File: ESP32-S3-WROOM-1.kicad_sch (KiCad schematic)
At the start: 24 parts, among them J11 Conn_01x08, J13 Conn_02x09_Top_Bottom, J14 Conn_01x09, J15 Conn_02x09_Top_Bottom, J4 JST-XH, J6 Conn_01x09, J7 Conn_02x20_Counter_Clockwise, J8 Conn_01x08, J9 Conn_01x08, SW4 SW_Push, U8 ESP32-S3-WROOM-1-N8R2

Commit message: Finished new board
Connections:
- net +5V: now also J4.4; no longer J4.1
- net Earth: now also J4.1; no longer J4.4
- net Pico_SCL1: now also U8.25 (GPIO48/SPICLK_N/SUBSPICLK_N_DIFF); no longer U8.26 (GPIO45)
- net Pico_SDA1: now also U8.26 (GPIO45); no longer U8.25 (GPIO48/SPICLK_N/SUBSPICLK_N_DIFF)
- net SCL: now also J4.3; no longer J4.2
- net SDA: now also J4.2; no longer J4.3
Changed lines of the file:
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@@
 	(wire
 		(pts
+			(xy 269.24 146.05) (xy 269.24 154.94)
+		)
+		(stroke
+			(width 0)
+			(type default)
+		)
+	)
+	(wire
+		(pts
 			(xy 143.51 59.69) (xy 149.86 59.69)
 		)
@@
 	(wire
 		(pts
-			(xy 269.24 146.05) (xy 269.24 154.94)
-		)
-		(stroke
-			(width 0)
-			(type default)
-		)
-	)
-	(wire
-		(pts
 			(xy 45.72 67.31) (xy 46.99 67.31)
 		)
@@
 	(global_label "Pico_SCL1"
 		(shape input)
-		(at 260.35 102.87 0)
+		(at 260.35 110.49 0)
 		(fields_autoplaced yes)
 		(effects
@@
 		)
 		(property "Intersheetrefs" "${INTERSHEET_REFS}"
-			(at 273.1323 102.87 0)
+			(at 273.1323 110.49 0)
 			(effects
 				(font
@@
 	(global_label "Pico_SDA1"
 		(shape input)
-		(at 260.35 110.49 0)
+		(at 260.35 102.87 0)
 		(fields_autoplaced yes)
 		(effects
@@
 		)
 		(property "Intersheetrefs" "${INTERSHEET_REFS}"
-			(at 273.1928 110.49 0)
+			(at 273.1928 102.87 0)
 			(effects
 				(font
@@
 		(exclude_from_sim no)
 		(in_bom yes)
-		(on_board yes)
+		(on_board no)
 		(dnp no)
 		(property "Reference" "C18"
@@
 		(exclude_from_sim no)
 		(in_bom yes)
-		(on_board yes)
+		(on_board no)
 		(dnp no)
 		(fields_autoplaced yes)
@@
 	)
 	(symbol
+		(lib_id "JST-ZH-4Pin:B4B-ZRLFSN")
+		(at 269.24 162.56 0)
+		(mirror x)
+		(unit 1)
+		(exclude_from_sim no)
+		(in_bom yes)
+		(on_board yes)
+		(dnp no)
+		(property "Reference" "J4"
+			(at 276.352 150.368 0)
+			(effects
+				(font
+					(size 1.524 1.524)
+				)
+				(justify left)
+			)
+		)
+		(property "Value" "JST-XH"
+			(at 282.702 157.48 0)
+			(effects
+				(font
+					(size 1.524 1.524)
+				)
+				(justify left)
+				(hide yes)
+			)
+		)
+		(property "Footprint" "Connector_JST:JST_XH_B4B-XH-A_1x04_P2.50mm_Vertical"
+			(at 269.24 162.56 0)
+			(effects
+				(font
+					(size 1.27 1.27)
+					(italic yes)
+				)
+				(hide yes)
+			)
+		)
+		(property "Datasheet" ""
+			(at 269.24 162.56 0)
+			(effects
+				(font
+					(size 1.27 1.27)
+					(italic yes)
+				)
+				(hide yes)
+			)
+		)
+		(property "Description" ""
+			(at 269.24 162.56 0)
+			(effects
+				(font
+					(size 1.27 1.27)
+				)
+				(hide yes)
+			)
+		)
+		(property "JLCPCB Rotation Offset" ""
+			(at 269.24 162.56 0)
+			(effects
+				(font
+					(size 1.27 1.27)
+				)
+				(hide yes)
+			)
+		)
+		(property "LCSC Part # " ""
+			(at -0.508 7.874 0)
+			(effects
+				(font
+					(size 1.27 1.27)
+				)
+				(hide yes)
+			)
+		)
+		(pin "2"
+		)
+		(pin "1"
+		)
+		(pin "3"
+		)
+		(pin "4"
+		)
+		(instances
+			(project "DeltaRhoRobot"
+				(path "/cced1a6d-3dc4-42b2-93bd-998a7b4cf4e8/5eb80655-957d-4a1c-8d7d-b2e173715026"
+					(reference "J4")
+					(unit 1)
+				)
+			)
+		)
+	)
+	(symbol
 		(lib_id "power:Earth")
 		(at 36.83 146.05 0)
@@
 		(exclude_from_sim no)
 		(in_bom yes)
-		(on_board yes)
+		(on_board no)
 		(dnp no)
 		(fields_autoplaced yes)
@@
 					(unit 1)
 				)
-			)
-		)
-	)
-	(symbol
-		(lib_id "JST-ZH-4Pin:B4B-ZRLFSN")
-		(at 269.24 154.94 0)
-		(unit 1)
-		(exclude_from_sim no)
-		(in_bom yes)
-		(on_board yes)
-		(dnp no)
-		(property "Reference" "J4"
-			(at 275.59 150.368 0)
-			(effects
-				(font
-					(size 1.524 1.524)
-				)
-				(justify left)
-			)
-		)
-		(property "Value" "JST-XH"
-			(at 282.702 160.02 0)
-			(effects
-				(font
-					(size 1.524 1.524)
-				)
-				(justify left)
-				(hide yes)
-			)
-		)
-		(property "Footprint" "Connector_JST:JST_XH_B4B-XH-A_1x04_P2.50mm_Vertical"
-			(at 269.24 154.94 0)
-			(effects
-				(font
-					(size 1.27 1.27)
-					(italic yes)
-				)
-				(hide yes)
-			)
-		)
-		(property "Datasheet" ""
-			(at 269.24 154.94 0)
-			(effects
-				(font
-					(size 1.27 1.27)
-					(italic yes)
-				)
-				(hide yes)
-			)
-		)
-		(property "Description" ""
-			(at 269.24 154.94 0)
-			(effects
-				(font
-					(size 1.27 1.27)
-				)
-				(hide yes)
-			)
-		)
-		(property "JLCPCB Rotation Offset" ""
-			(at 269.24 154.94 0)
-			(effects
-				(font
-					(size 1.27 1.27)
-				)
-				(hide yes)
-			)
-		)
-		(property "LCSC Part # " ""
-			(at -0.508 309.626 0)
-			(effects
-				(font
-					(size 1.27 1.27)
-				)
-				(hide yes)
-			)
-		)
-		(pin "2"
-		)
-		(pin "1"
-		)
-		(pin "3"
-		)
-		(pin "4"
-		)
-		(instances
-			(project "DeltaRhoRobot"
-				(path "/cced1a6d-3dc4-42b2-93bd-998a7b4cf4e8/5eb80655-957d-4a1c-8d7d-b2e173715026"
-					(reference "J4")
-					(unit 1)
-				)

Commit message: Graphics
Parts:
- renumbered C32 to C10, C16 to C2, C15 to C3, C17 to C4, C19 to C5, C21 to C6, C22 to C7, C20 to C9, D7 to D1, D6 to D2, J13 to J1, J7 to J12, J6 to J2, J14 to J3, J15 to J4, J11 to J7, J9 to J8, J4 to J9, R20 to R17, R21 to R18, U8 to U1
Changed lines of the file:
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@@
 		(on_board yes)
 		(dnp no)
-		(property "Reference" "C22"
+		(property "Reference" "C7"
 			(at 106.045 102.235 0)
 			(effects
@@
 			(project "DeltaRhoRobot"
 				(path "/cced1a6d-3dc4-42b2-93bd-998a7b4cf4e8/5eb80655-957d-4a1c-8d7d-b2e173715026"
-					(reference "C22")
+					(reference "C7")
 					(unit 1)
 				)
@@
 		(dnp no)
 		(fields_autoplaced yes)
-		(property "Reference" "C32"
+		(property "Reference" "C10"
 			(at 45.7263 16.764 90)
 			(effects
@@
 			(project "DeltaRhoRobot"
 				(path "/cced1a6d-3dc4-42b2-93bd-998a7b4cf4e8/5eb80655-957d-4a1c-8d7d-b2e173715026"
-					(reference "C32")
+					(reference "C10")
 					(unit 1)
 				)
@@
 		(dnp no)
 		(fields_autoplaced yes)
-		(property "Reference" "R20"
+		(property "Reference" "R17"
 			(at 249.555 151.13 0)
 			(effects
@@
 			(project "DeltaRhoRobot"
 				(path "/cced1a6d-3dc4-42b2-93bd-998a7b4cf4e8/5eb80655-957d-4a1c-8d7d-b2e173715026"
-					(reference "R20")
+					(reference "R17")
 					(unit 1)
 				)
@@
 		(on_board yes)
 		(dnp no)
-		(property "Reference" "D7"
+		(property "Reference" "D1"
 			(at 58.42 31.115 0)
 			(effects
@@
 			(project "DeltaRhoRobot"
 				(path "/cced1a6d-3dc4-42b2-93bd-998a7b4cf4e8/5eb80655-957d-4a1c-8d7d-b2e173715026"
-					(reference "D7")
+					(reference "D1")
 					(unit 1)
 				)
@@
 		(dnp no)
 		(fields_autoplaced yes)
-		(property "Reference" "J11"
+		(property "Reference" "J7"
 			(at 144.78 168.275 0)
 			(effects
@@
 			(project "DeltaRhoRobot"
 				(path "/cced1a6d-3dc4-42b2-93bd-998a7b4cf4e8/5eb80655-957d-4a1c-8d7d-b2e173715026"
-					(reference "J11")
+					(reference "J7")
 					(unit 1)
 				)
@@
 		(on_board yes)
 		(dnp no)
-		(property "Reference" "J15"
+		(property "Reference" "J4"
 			(at 103.505 44.45 0)
 			(effects
@@
 			(project "DeltaRhoRobot"
 				(path "/cced1a6d-3dc4-42b2-93bd-998a7b4cf4e8/5eb80655-957d-4a1c-8d7d-b2e173715026"
-					(reference "J15")
+					(reference "J4")
 					(unit 1)
 				)
@@
 		(on_board yes)
 		(dnp no)
-		(property "Reference" "J6"
+		(property "Reference" "J2"
 			(at 127.635 97.79 0)
 			(effects
@@
 			(project "DeltaRhoRobot"
 				(path "/cced1a6d-3dc4-42b2-93bd-998a7b4cf4e8/5eb80655-957d-4a1c-8d7d-b2e173715026"
-					(reference "J6")
+					(reference "J2")
 					(unit 1)
 				)
@@
 		(dnp no)
 		(fields_autoplaced yes)
-		(property "Reference" "C17"
+		(property "Reference" "C4"
 			(at 224.79 25.3936 0)
 			(effects
@@
 			(project "DeltaRhoRobot"
 				(path "/cced1a6d-3dc4-42b2-93bd-998a7b4cf4e8/5eb80655-957d-4a1c-8d7d-b2e173715026"
-					(reference "C17")
+					(reference "C4")
 					(unit 1)
 				)
@@
 		(dnp no)
 		(fields_autoplaced yes)
-		(property "Reference" "R21"
+		(property "Reference" "R18"
 			(at 262.255 152.4 0)
 			(effects
@@
 			(project "DeltaRhoRobot"
 				(path "/cced1a6d-3dc4-42b2-93bd-998a7b4cf4e8/5eb80655-957d-4a1c-8d7d-b2e173715026"
-					(reference "R21")
+					(reference "R18")
 					(unit 1)
 				)
@@
 		(on_board yes)
 		(dnp no)
-		(property "Reference" "C19"
+		(property "Reference" "C5"
 			(at 90.805 102.235 0)
 			(effects
@@
 			(project "DeltaRhoRobot"
 				(path "/cced1a6d-3dc4-42b2-93bd-998a7b4cf4e8/5eb80655-957d-4a1c-8d7d-b2e173715026"
-					(reference "C19")
+					(reference "C5")
 					(unit 1)
 				)
@@
 		(on_board yes)
 		(dnp no)
-		(property "Reference" "J4"
+		(property "Reference" "J9"
 			(at 276.352 150.368 0)
 			(effects
@@
 			(project "DeltaRhoRobot"
 				(path "/cced1a6d-3dc4-42b2-93bd-998a7b4cf4e8/5eb80655-957d-4a1c-8d7d-b2e173715026"
-					(reference "J4")
+					(reference "J9")
 					(unit 1)
 				)
@@
 		(on_board yes)
 		(dnp no)
-		(property "Reference" "J9"
+		(property "Reference" "J8"
 			(at 46.355 127 0)
 			(effects
@@
 			(project "DeltaRhoRobot"
 				(path "/cced1a6d-3dc4-42b2-93bd-998a7b4cf4e8/5eb80655-957d-4a1c-8d7d-b2e173715026"
-					(reference "J9")
+					(reference "J8")
 					(unit 1)
 				)
@@
 		(on_board yes)
 		(dnp no)
-		(property "Reference" "J13"
+		(property "Reference" "J1"
 			(at 121.285 125.73 0)
 			(effects
@@
 			(project "DeltaRhoRobot"
 				(path "/cced1a6d-3dc4-42b2-93bd-998a7b4cf4e8/5eb80655-957d-4a1c-8d7d-b2e173715026"
-					(reference "J13")
+					(reference "J1")
 					(unit 1)
 				)
@@
 		(on_board yes)
 		(dnp no)
-		(property "Reference" "J7"
+		(property "Reference" "J12"
 			(at 39.37 60.96 0)
 			(effects
@@
 			(project "DeltaRhoRobot"
 				(path "/cced1a6d-3dc4-42b2-93bd-998a7b4cf4e8/5eb80655-957d-4a1c-8d7d-b2e173715026"
-					(reference "J7")
+					(reference "J12")
 					(unit 1)
 				)
@@
 		(on_board yes)
 		(dnp no)
-		(property "Reference" "C21"
+		(property "Reference" "C6"
 			(at 100.965 102.235 0)
 			(effects
@@
 			(project "DeltaRhoRobot"
 				(path "/cced1a6d-3dc4-42b2-93bd-998a7b4cf4e8/5eb80655-957d-4a1c-8d7d-b2e173715026"
-					(reference "C21")
+					(reference "C6")
 					(unit 1)
 				)
@@
 		(on_board yes)
 		(dnp no)
-		(property "Reference" "U8"
+		(property "Reference" "U1"
 			(at 171.45 31.75 0)
 			(effects
@@
 			(project "DeltaRhoRobot"
 				(path "/cced1a6d-3dc4-42b2-93bd-998a7b4cf4e8/5eb80655-957d-4a1c-8d7d-b2e173715026"
-					(reference "U8")
+					(reference "U1")
 					(unit 1)
 				)
@@
 		(on_board yes)
 		(dnp no)
-		(property "Reference" "C16"
+		(property "Reference" "C2"
 			(at 215.9 26.67 0)
 			(effects
@@
 			(project "DeltaRhoRobot"
 				(path "/cced1a6d-3dc4-42b2-93bd-998a7b4cf4e8/5eb80655-957d-4a1c-8d7d-b2e173715026"
-					(reference "C16")
+					(reference "C2")
 					(unit 1)
 				)
@@
 		(on_board yes)
 		(dnp no)
-		(property "Reference" "C20"
+		(property "Reference" "C9"
 			(at 95.885 102.235 0)
 			(effects
@@
 			(project "DeltaRhoRobot"
 				(path "/cced1a6d-3dc4-42b2-93bd-998a7b4cf4e8/5eb80655-957d-4a1c-8d7d-b2e173715026"
-					(reference "C20")
+					(reference "C9")
 					(unit 1)
 				)
@@
 		(dnp no)
 		(fields_autoplaced yes)
-		(property "Reference" "D6"
+		(property "Reference" "D2"
 			(at 38.1 33.1821 0)
 			(effects
@@
 			(project "DeltaRhoRobot"
 				(path "/cced1a6d-3dc4-42b2-93bd-998a7b4cf4e8/5eb80655-957d-4a1c-8d7d-b2e173715026"
-					(reference "D6")
+					(reference "D2")
 					(unit 1)
 				)
@@
 		(on_board yes)
 		(dnp no)
-		(property "Reference" "J14"
+		(property "Reference" "J3"
 			(at 90.424 43.18 0)
 			(effects
@@
 			(project "DeltaRhoRobot"
 				(path "/cced1a6d-3dc4-42b2-93bd-998a7b4cf4e8/5eb80655-957d-4a1c-8d7d-b2e173715026"
-					(reference "J14")
+					(reference "J3")
 					(unit 1)
 				)
@@
 		(on_board yes)
 		(dnp no)
-		(property "Reference" "C15"
+		(property "Reference" "C3"
 			(at 198.12 26.67 0)
 			(effects
@@
 			(project "DeltaRhoRobot"
 				(path "/cced1a6d-3dc4-42b2-93bd-998a7b4cf4e8/5eb80655-957d-4a1c-8d7d-b2e173715026"
-					(reference "C15")
+					(reference "C3")
 					(unit 1)
 				)

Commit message: Draft power redo
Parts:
- removed C18: 100nF, Capacitor_SMD:C_0402_1005Metric, symbol Device:C_Small
- removed J8: Conn_01x08, Connector_PinSocket_2.54mm:PinSocket_1x08_P2.54mm_Vertical, symbol Connector_Generic:Conn_01x08
- removed SW4: SW_Push, Button_Switch_SMD:SW_SPST_PTS810, symbol Switch:SW_Push
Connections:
- no-connect marks 31 -> 32
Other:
- removed sheet ESP32CAM
- note removed: "ESP32-CAM"
- moved on the sheet: J8

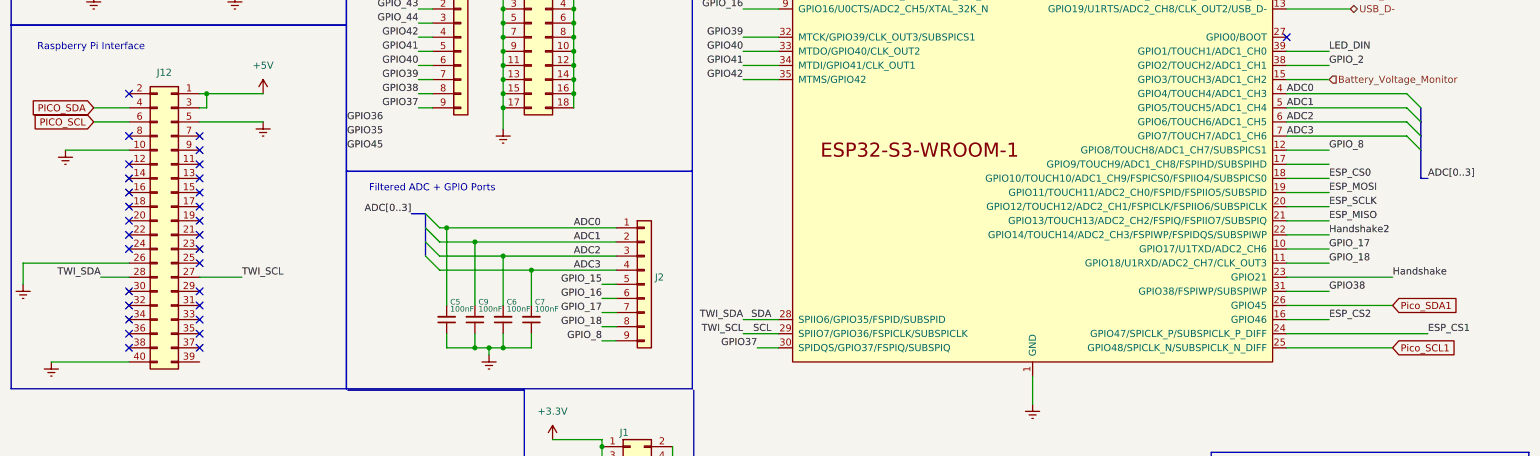
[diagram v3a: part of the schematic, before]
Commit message: Adding UART backup
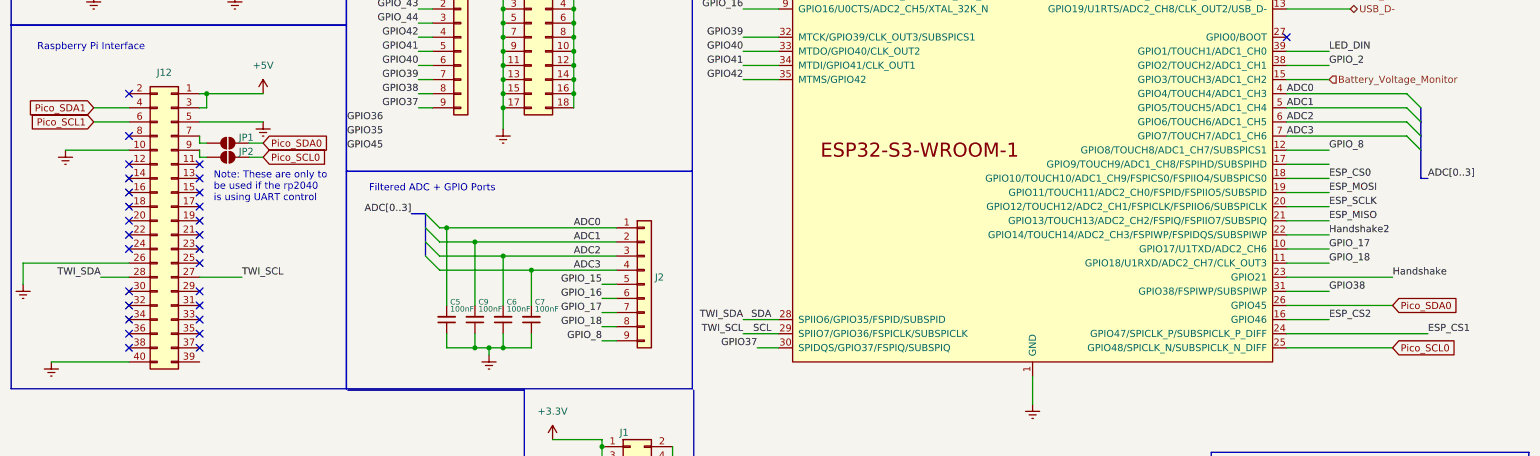
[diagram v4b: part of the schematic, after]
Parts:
- added JP1, JP2: SolderJumper_2_Open, Jumper:SolderJumper-2_P1.3mm_Open_RoundedPad1.0x1.5mm, symbol Jumper:SolderJumper_2_Open
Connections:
- net PICO_SCL is gone; now on net Pico_SCL1: J12.6 (Pin_6)
- net PICO_SDA is gone; now on net Pico_SDA1: J12.4 (Pin_4)
- net Pico_SCL1: no longer U1.25 (GPIO48/SPICLK_N/SUBSPICLK_N_DIFF)
- net Pico_SDA1: no longer U1.26 (GPIO45)
- net at J12.7 (Pin_7): now also JP1.1 (A)
- net at J12.9 (Pin_9): now also JP2.1 (A)
- new net Pico_SCL0: JP2.2 (B), U1.25 (GPIO48/SPICLK_N/SUBSPICLK_N_DIFF)
- new net Pico_SDA0: JP1.2 (B), U1.26 (GPIO45)
- no-connect marks 32 -> 30
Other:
- note added: "Note: These are only to be used if the rp2040 is using UART control"
